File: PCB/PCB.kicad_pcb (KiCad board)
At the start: 2 copper layers, 17 parts, among them SW1 SW_Push, SW2 SW_Push, SW3 SW_Push, SW4 SW_Push, SW5 SW_Push, SW6 SW_Push, U1 NodeMCU_1.0_(ESP-12E)

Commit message: minor tweek and started with PCB layout
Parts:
- moved EM4100 84.1 mm to (85.0, 61.5)
- moved SW2 82.9 mm to (211.5, 123.5)
- moved D1 80.1 mm to (84.5, 40.5)
- moved D2 69.3 mm to (192.7, 38.5)
- moved SW1 69.0 mm to (194.0, 123.5)
- moved BZ1 61.4 mm to (184.9, 58.5)
- moved SW4 43.3 mm to (162.5, 147.0)
- moved SW5 38.3 mm to (151.5, 157.0)
- moved SW3 33.9 mm to (151.0, 137.0)
- moved SW6 17.5 mm to (139.5, 147.5)
- moved R3 12.6 mm to (148.4, 106.3)
- moved R5 12.6 mm to (148.4, 112.9)
- moved R2 12.6 mm to (148.4, 103.0)
- moved R4 12.6 mm to (148.4, 109.6)
- moved R1 11.6 mm to (148.5, 98.0)
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
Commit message: started PCB drawing
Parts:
- moved EM4100 44.2 mm to (99.6, 103.2), turned to -90 degrees
- moved BZ1 42.0 mm to (174.8, 99.3)
- moved SW2 34.9 mm to (177.3, 130.4)
- moved R2 33.4 mm to (179.6, 115.2), turned to -90 degrees
- moved SW1 31.5 mm to (163.2, 130.4)
- moved U1 26.2 mm to (133.5, 104.3)
- moved R3 26.1 mm to (173.1, 115.1), turned to -90 degrees
- moved SW4 24.7 mm to (144.1, 130.4)
- moved SW5 24.7 mm to (137.1, 137.0)
- moved SW6 19.5 mm to (130.1, 130.4)
- moved R4 19.4 mm to (167.0, 115.2), turned to -90 degrees
- moved SW3 19.1 mm to (137.1, 124.0)
- moved R5 13.2 mm to (161.4, 115.1), turned to -90 degrees
- moved R1 13.1 mm to (161.5, 99.5), turned to -90 degrees
- moved D2 12.5 mm to (181.2, 33.6)
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- renumbered NHD-C12864A1Z-FSW-FBW-HTT1 to NHD
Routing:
- net Net-(D1-A): track 0.00 -> 139.7 mm
- net Net-(SW3-Pad1): track 0.00 -> 118.5 mm
- net Net-(EM4100-TX): track 0.00 -> 106.3 mm
- net Net-(EM4100-RX): track 0.00 -> 97.7 mm
- net Net-(NHD-C12864A1Z-FSW-FBW-HTT1-~{RESET}): track 0.00 -> 91.7 mm
- net Net-(NHD-C12864A1Z-FSW-FBW-HTT1-~{CS}): track 0.00 -> 70.6 mm
- net VCC: track 0.00 -> 66.5 mm
- net Net-(NHD-C12864A1Z-FSW-FBW-HTT1-A0): track 0.00 -> 66.3 mm
- net Net-(NHD-C12864A1Z-FSW-FBW-HTT1-SI): track 0.00 -> 58.3 mm
- net Net-(NHD-C12864A1Z-FSW-FBW-HTT1-LED+): track 0.00 -> 57.5 mm
- net Net-(NHD-C12864A1Z-FSW-FBW-HTT1-SCL): track 0.00 -> 51.7 mm
- net Net-(R2-Pad2): track 0.00 -> 45.7 mm
- net /Analog buttons: track 0.00 -> 45.3 mm
- net Net-(R4-Pad2): track 0.00 -> 38.9 mm
- net Net-(R5-Pad2): track 0.00 -> 36.3 mm
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- added copper zone on B.Cu, net GND

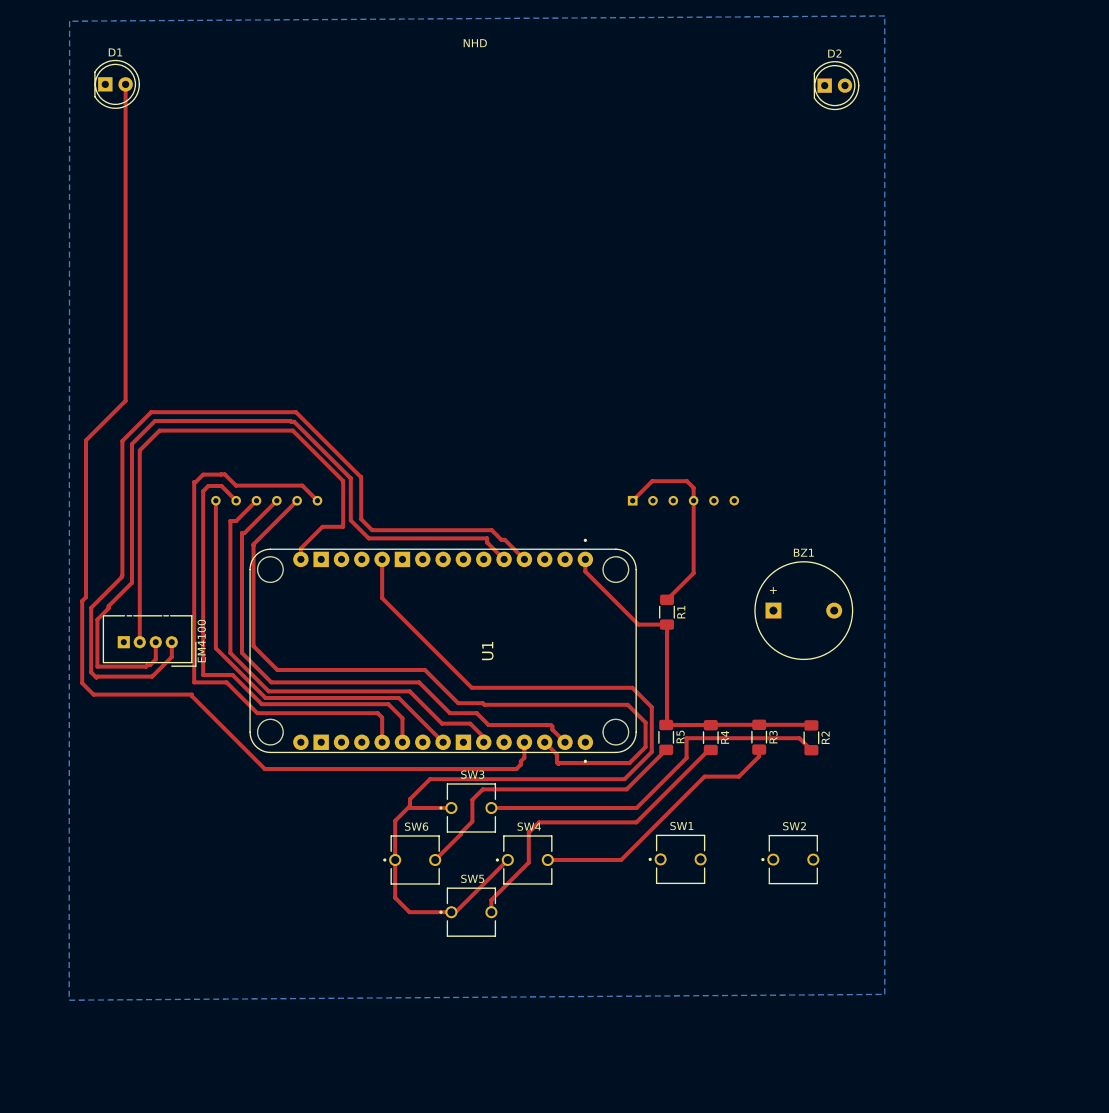
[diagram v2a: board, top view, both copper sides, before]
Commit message: done pcb drawing
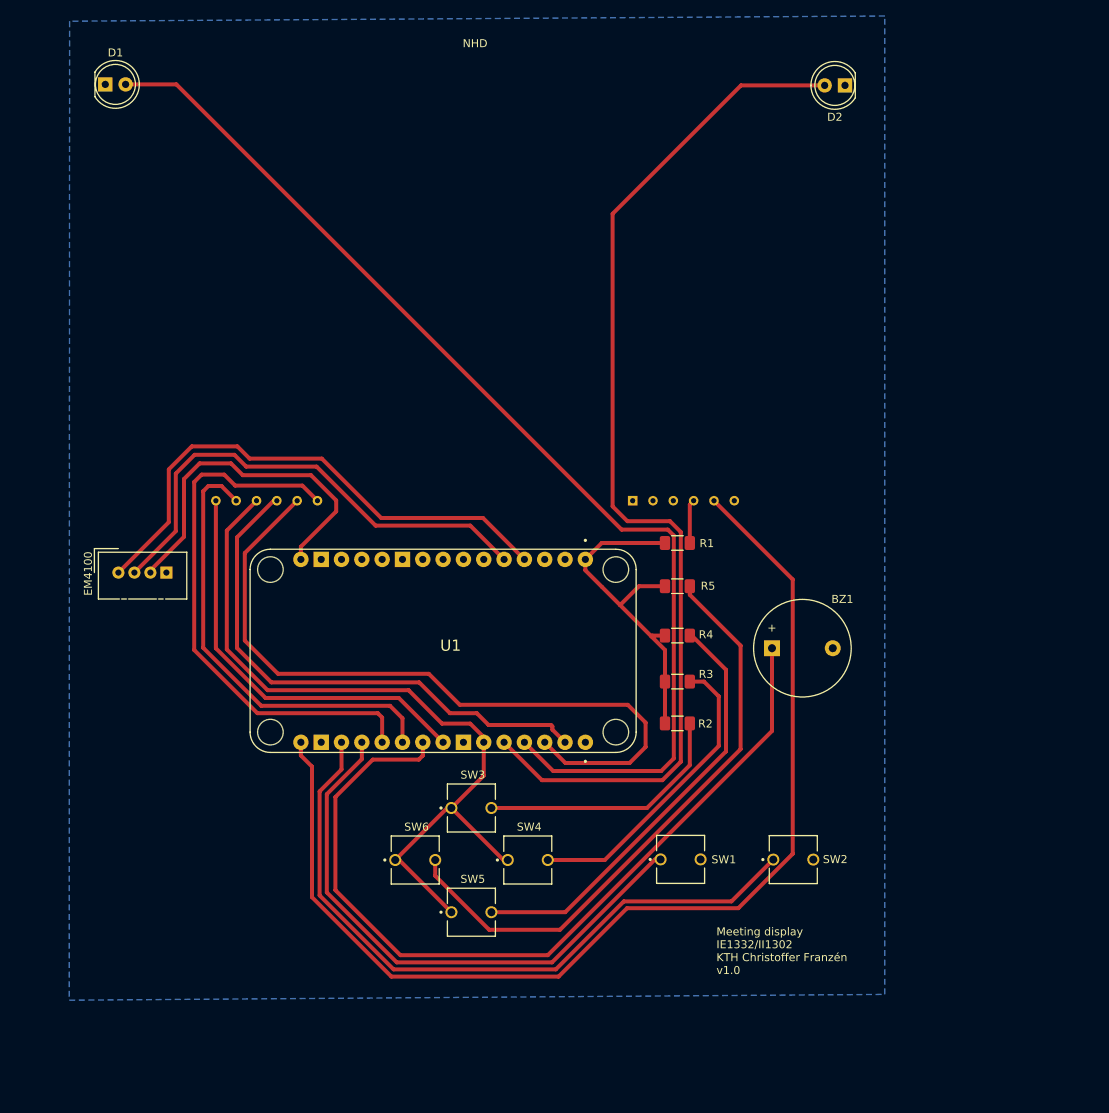
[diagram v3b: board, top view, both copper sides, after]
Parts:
- moved R5 19.0 mm to (162.8, 96.2), turned to 0 degrees
- moved R2 16.8 mm to (162.8, 113.4), turned to 0 degrees
- moved R4 13.4 mm to (162.8, 102.4), turned to 0 degrees
- moved R3 12.4 mm to (162.8, 108.2), turned to 0 degrees
- moved EM4100 11.0 mm to (93.0, 94.5), turned to 90 degrees
- moved R1 8.75 mm to (162.8, 90.8), turned to 180 degrees
- moved BZ1 4.70 mm to (174.7, 104.0)
- moved D2 2.54 mm to (183.8, 33.6), turned to 180 degrees
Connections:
- NHD pad 3: Net-(NHD-C12864A1Z-FSW-FBW-HTT1-LED+) -> Net-(NHD-C12864A1Z-FSW-FBW-HTT1-VDD)
- SW3 pad 1: Net-(SW3-Pad1) -> Net-(NHD-C12864A1Z-FSW-FBW-HTT1-VDD)
- SW4 pad 1: Net-(SW3-Pad1) -> Net-(NHD-C12864A1Z-FSW-FBW-HTT1-VDD)
- SW5 pad 1: Net-(SW3-Pad1) -> Net-(NHD-C12864A1Z-FSW-FBW-HTT1-VDD)
- SW6 pad 1: Net-(SW3-Pad1) -> Net-(NHD-C12864A1Z-FSW-FBW-HTT1-VDD)
- U1 pad 11: Net-(SW3-Pad1) -> unconnected-(U1-3.3V-Pad11)
- U1 pad 16: unconnected-(U1-3.3V-Pad16) -> Net-(NHD-C12864A1Z-FSW-FBW-HTT1-LED+)
- U1 pad 25: Net-(NHD-C12864A1Z-FSW-FBW-HTT1-LED+) -> Net-(NHD-C12864A1Z-FSW-FBW-HTT1-VDD)
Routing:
- net Net-(D2-A): track 0.00 -> 133.3 mm
- net Net-(SW3-Pad1): track 118.5 -> 0.00 mm
- net Net-(BZ1-+): track 0.00 -> 106.3 mm
- net Net-(NHD-C12864A1Z-FSW-FBW-HTT1-VDD): track 0.00 -> 97.0 mm
- net Net-(U1-TX(GPIO1)): track 0.00 -> 86.5 mm
- net Net-(NHD-C12864A1Z-FSW-FBW-HTT1-LED+): track 57.5 -> 138.7 mm
- net Net-(U1-RX(DPIO3)): track 0.00 -> 71.3 mm
- net Net-(EM4100-TX): track 106.3 -> 67.0 mm
- net Net-(R5-Pad2): track 36.3 -> 75.3 mm
- net Net-(EM4100-RX): track 97.7 -> 61.9 mm
- net VCC: track 66.5 -> 44.4 mm
- net GND: track 24.3 -> 5.48 mm
- net Net-(R4-Pad2): track 38.9 -> 54.2 mm
- net Net-(R2-Pad2): track 45.7 -> 32.3 mm
- net Net-(R3-Pad2): track 32.6 -> 37.9 mm
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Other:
- board text added: "Meeting display IE1332/II1302 KTH Christoffer Franzén v1.0"

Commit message: fixed edge cuts and fixed all warnings
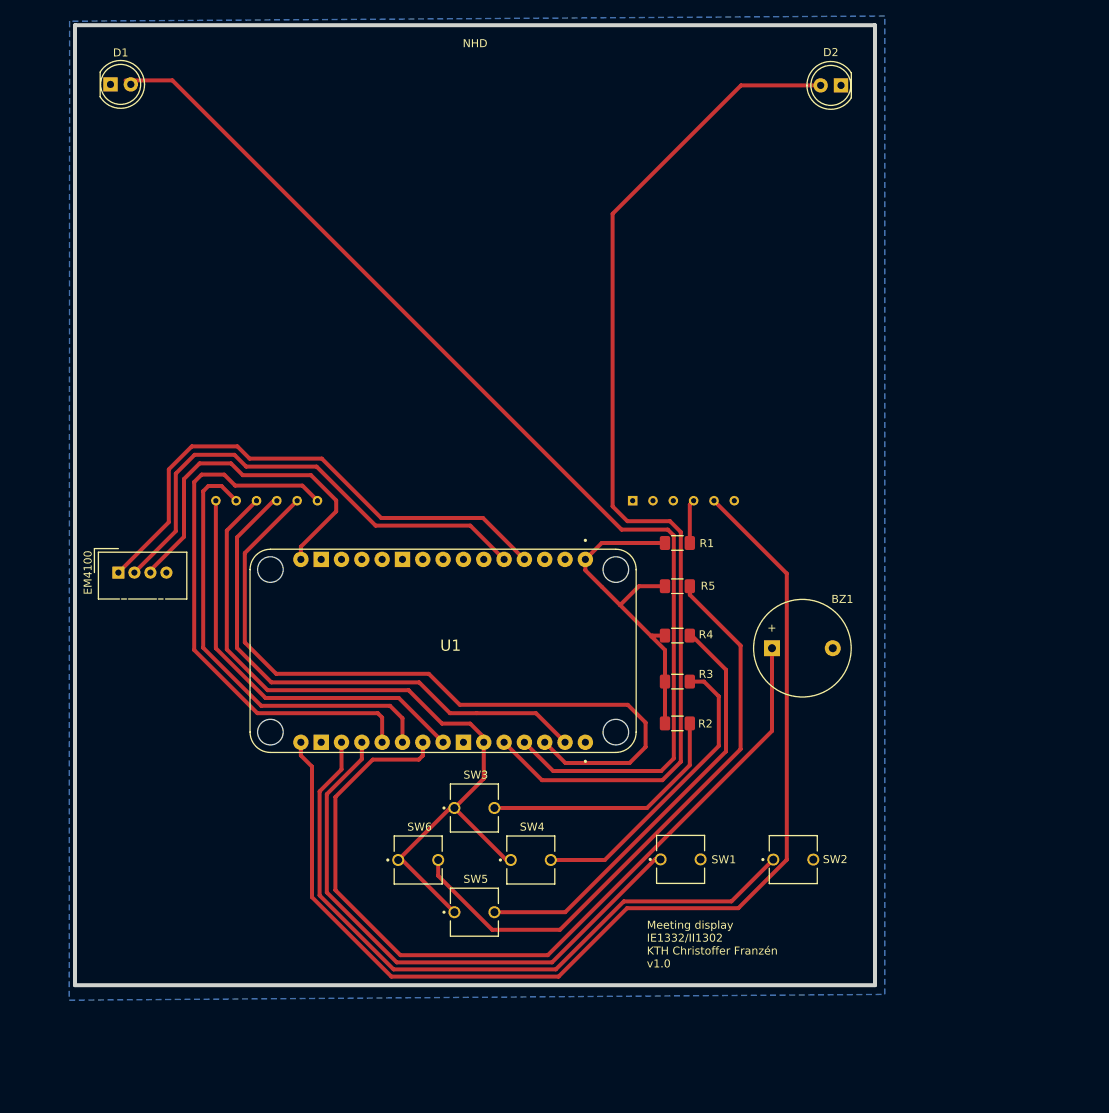
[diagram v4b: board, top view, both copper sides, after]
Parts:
- moved D1 0.65 mm to (92.0, 33.5)
- moved D2 0.50 mm to (183.3, 33.6)
- moved SW3 0.38 mm to (137.4, 124.0)
- moved SW4 0.38 mm to (144.5, 130.4)
- moved SW5 0.38 mm to (137.4, 137.0)
- moved SW6 0.38 mm to (130.4, 130.4)
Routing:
- net Net-(D2-A): track 133.3 -> 132.3 mm
- net Net-(NHD-C12864A1Z-FSW-FBW-HTT1-LED+): track 138.7 -> 138.1 mm
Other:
- board outline added: 100 x 120 mm

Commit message: added mounting holes and gerber files
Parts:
- moved D1 4.77 mm to (91.5, 38.2)
- moved D2 4.59 mm to (183.6, 38.2)
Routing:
- net Net-(D1-A): track 140.8 -> 139.3 mm
- net Net-(D2-A): track 132.3 -> 133.4 mm
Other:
- outline, holes or cut-outs redrawn
- board text added: "Meeting display v1.0 IE1332/II1302 KTH Christoffer Franzén 2024-04-22"
- board text removed: "Meeting display IE1332/II1302 KTH Christoffer Franzén v1.0"
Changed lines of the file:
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@@
 			(plot_on_all_layers_selection 0x0000000_00000000)
 			(disableapertmacros no)
-			(usegerberextensions no)
+			(usegerberextensions yes)
 			(usegerberattributes yes)
 			(usegerberadvancedattributes yes)
-			(creategerberjobfile yes)
+			(creategerberjobfile no)
 			(dashed_line_dash_ratio 12.000000)
 			(dashed_line_gap_ratio 3.000000)
@@
 			(psa4output no)
 			(plotreference yes)
-			(plotvalue yes)
+			(plotvalue no)
 			(plotfptext yes)
 			(plotinvisibletext no)
 			(sketchpadsonfab no)
-			(subtractmaskfromsilk no)
+			(subtractmaskfromsilk yes)
 			(outputformat 1)
 			(mirror no)
-			(drillshape 1)
+			(drillshape 0)
 			(scaleselection 1)
-			(outputdirectory "")
+			(outputdirectory "gerbers/")
 		)
 	)
@@
 	(footprint "LED_THT:LED_D5.0mm"
 		(layer "F.Cu")
-		(at 91.96 33.5)
+		(at 91.475 38.25)
 		(descr "LED, diameter 5.0mm, 2 pins, http://cdn-reichelt.de/documents/datenblatt/A500/LL-504BC2E-009.pdf")
 		(tags "LED diameter 5.0mm 2 pins")
@@
 	(footprint "LED_THT:LED_D5.0mm"
 		(layer "F.Cu")
-		(at 183.275 33.625 180)
+		(at 183.6 38.2 180)
 		(descr "LED, diameter 5.0mm, 2 pins, http://cdn-reichelt.de/documents/datenblatt/A500/LL-504BC2E-009.pdf")
 		(tags "LED diameter 5.0mm 2 pins")
 		(property "Reference" "D2"
-			(at 1.275 4.125 180)
+			(at 1.225 4.15 180)
 			(layer "F.SilkS")
 			(effects
@@
 		)
 		(property "Value" "GREEN"
-			(at 1.275 -4.375 180)
+			(at 1.225 -4.35 180)
 			(layer "F.Fab")
 			(effects
@@
 		)
 		(fp_text user "${REFERENCE}"
-			(at 1.25 0 180)
+			(at 1.2 0.025 180)
 			(layer "F.Fab")
 			(effects
@@
 		(layer "Edge.Cuts")
 	)
-	(gr_text "Meeting display\nIE1332/II1302\nKTH Christoffer Franzén\nv1.0"
-		(at 159 144 0)
+	(gr_circle
+		(center 183.95 142.55)
+		(end 185.45 142.55)
+		(stroke
+			(width 0.05)
+			(type default)
+		)
+		(fill none)
+		(layer "Edge.Cuts")
+	)
+	(gr_circle
+		(center 91.075 142.55)
+		(end 92.575 142.55)
+		(stroke
+			(width 0.05)
+			(type default)
+		)
+		(fill none)
+		(layer "Edge.Cuts")
+	)
+	(gr_circle
+		(center 91.1 29.65)
+		(end 92.6 29.65)
+		(stroke
+			(width 0.05)
+			(type default)
+		)
+		(fill none)
+		(layer "Edge.Cuts")
+	)
+	(gr_circle
+		(center 183.95 29.65)
+		(end 185.45 29.65)
+		(stroke
+			(width 0.05)
+			(type default)
+		)
+		(fill none)
+		(layer "Edge.Cuts")
+	)
+	(gr_text "Meeting display v1.0\nIE1332/II1302\nKTH Christoffer Franzén\n2024-04-22"
+		(at 157.35 144.15 0)
 		(layer "F.SilkS")
 		(effects
@@
 	)
 	(segment
-		(start 160.8 119.325)
-		(end 147.29 119.325)
+		(start 150.615 89.15)
+		(end 99.215 37.75)
 		(width 0.5)
 		(layer "F.Cu")
@@
 	)
 	(segment
-		(start 155.85 89.15)
-		(end 161.621878 89.15)
+		(start 143.7 115.735)
+		(end 147.29 119.325)
 		(width 0.5)
 		(layer "F.Cu")
@@
 	)
 	(segment
-		(start 161.621878 89.15)
-		(end 162.375 89.903122)
+		(start 99.215 37.75)
+		(end 93.365 37.75)
 		(width 0.5)
 		(layer "F.Cu")
@@
 	)
 	(segment
-		(start 162.375 89.903122)
+		(start 160.8 119.325)
 		(end 162.375 117.75)
 		(width 0.5)
@@
 	)
 	(segment
-		(start 93.85 33)
-		(end 99.7 33)
+		(start 162.375 89.903122)
+		(end 161.621878 89.15)
 		(width 0.5)
 		(layer "F.Cu")
@@
 	)
 	(segment
-		(start 99.7 33)
-		(end 155.85 89.15)
+		(start 161.621878 89.15)
+		(end 150.615 89.15)
 		(width 0.5)
 		(layer "F.Cu")
@@
 	(segment
 		(start 147.29 119.325)
-		(end 143.7 115.735)
+		(end 160.8 119.325)
 		(width 0.5)
 		(layer "F.Cu")
@@
 	(segment
 		(start 162.375 117.75)
-		(end 160.8 119.325)
+		(end 162.375 89.903122)
 		(width 0.5)
 		(layer "F.Cu")
@@
 	)
 	(segment
-		(start 161.9 88.1)
-		(end 156.575 88.1)
+		(start 154.725 45.975)
+		(end 162.5 38.2)
 		(width 0.5)
 		(layer "F.Cu")
@@
 	)
 	(segment
-		(start 145.9 120.475)
-		(end 160.95 120.475)
+		(start 156.575 88.1)
+		(end 154.725 86.25)
 		(width 0.5)
 		(layer "F.Cu")
@@
 	)
 	(segment
-		(start 163.25 89.45)
-		(end 161.9 88.1)
+		(start 154.725 86.25)
+		(end 154.725 45.975)
 		(width 0.5)
 		(layer "F.Cu")
@@
 	)
 	(segment
-		(start 154.725 49.675)
-		(end 170.775 33.625)
+		(start 141.16 115.735)
+		(end 145.9 120.475)
 		(width 0.5)
 		(layer "F.Cu")
@@
 	)
 	(segment
-		(start 141.16 115.735)
-		(end 145.9 120.475)
+		(start 162.5 38.2)
+		(end 181.06 38.2)
 		(width 0.5)
 		(layer "F.Cu")
@@
 	)
 	(segment
-		(start 156.575 88.1)
-		(end 154.725 86.25)
+		(start 161.9 88.1)
+		(end 156.575 88.1)
 		(width 0.5)
 		(layer "F.Cu")
@@
 	)
 	(segment
-		(start 170.775 33.625)
-		(end 180.235 33.625)
+		(start 163.25 89.45)
+		(end 161.9 88.1)
 		(width 0.5)
 		(layer "F.Cu")
@@
 	)
 	(segment
-		(start 163.25 118.175)
-		(end 163.25 89.45)
+		(start 145.9 120.475)
+		(end 160.95 120.475)
 		(width 0.5)
 		(layer "F.Cu")
@@
 	)
 	(segment
-		(start 154.725 86.25)
-		(end 154.725 49.675)
+		(start 163.25 118.175)
+		(end 163.25 89.45)
 		(width 0.5)
 		(layer "F.Cu")
